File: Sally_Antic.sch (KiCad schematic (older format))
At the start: 0 parts

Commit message: GTIA
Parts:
- added C30, C31: 100nF, Atari:C_Axial_L5.1mm_D2.5mm_P12.50mm_Horizontal, symbol Device:C
- added R31: 3k, Atari:R_Axial_DIN0207_L3.6mm_D2.2mm_P10.16mm_Horizontal, symbol Device:R
- added U18: 74LS08, Package_DIP:DIP-14_W7.62mm_Socket, symbol 74xx:74LS08
- added U7: Antic, Package_DIP:DIP-40_W15.24mm_Socket, symbol Atari:Antic
- added U8: Sally, Package_DIP:DIP-40_W15.24mm_Socket, symbol Atari:Sally
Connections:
- new net: U18.4, U18.5, U7.34 (O0)
- new net: R31.2, U7.6 (~RNMI)
- new net +5VA: C30.1, C31.1, R31.1, U7.21 (VCC), U8.8 (VCC)
- new net A0: U7.13 (A0), U8.9 (A0)
- new net A1: U7.12 (A1), U8.10 (A1)
- new net A10: U7.16 (A10), U8.19 (A10)
- new net A11: U7.22 (A11), U8.20 (A11)
- new net A12: U7.17 (A12), U8.22 (A12)
- new net A13: U7.18 (A13), U8.23 (A13)
- new net A14: U7.19 (A14), U8.24 (A14)
- new net A15: U7.20 (A15), U8.25 (A15)
- new net A2: U7.11 (A2), U8.11 (A2)
- new net A3: U7.10 (A3), U8.12 (A3)
- new net A4: U7.28 (A4), U8.13 (A4)
- new net A5: U7.27 (A5), U8.14 (A5)
- new net A6: U7.26 (A6), U8.15 (A6)
- new net A7: U7.25 (A7), U8.16 (A7)
- new net A8: U7.24 (A8), U8.17 (A8)
- new net A9: U7.23 (A9), U8.18 (A9)
- new net AN0: U7.2 (AN0)
- new net AN1: U7.3 (AN1)
- new net AN2: U7.5 (AN2)
- new net BO2: U7.29 (O2)
- new net D0: U7.30 (D0), U8.33 (D0)
- new net D1: U7.31 (D1), U8.32 (D1)
- new net D2: U7.32 (D2), U8.31 (D2)
- new net D3: U7.33 (D3), U8.30 (D3)
- new net D4: U7.40 (D4), U8.29 (D4)
- new net D5: U7.39 (D5), U8.28 (D5)
- new net D6: U7.38 (D6), U8.27 (D6)
- new net D7: U7.37 (D7), U8.26 (D7)
- new net GND: C30.2, C31.2, U7.1 (VSS), U8.1 (VSS), U8.21 (VSS), U8.38 (S0)
- new net HALT: U7.9 (~HALT), U8.35 (~HALT)
- new net IRQ: U8.4 (~IRQ)
- new net LP: U7.4 (~LP)
- new net NMI: U7.7 (~NMI), U8.6 (~NMI)
- new net O0: U18.6, U8.37 (O0)
- new net O1: U8.3 (O1)
- new net O2: U8.39 (O2)
- new net RDY: U7.15 (RDY), U8.2 (RDY)
- new net REF: U7.8 (~REF)
- new net RST: U7.36 (RST), U8.40 (~RST)
- new net RW: U7.14 (R/~W), U8.36 (R/~W)
- no-connect marks 0 -> 1

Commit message: MMU, Joy, Cart and Video
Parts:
- added R21, R22, R34: 3k, Atari:R_Axial_DIN0207_L3.6mm_D2.2mm_P10.16mm_Horizontal, symbol Device:R
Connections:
- net +5VA: now also R21.1, R22.1, R34.1
- net IRQ: now also R22.2
- net NMI: now also R21.2
- net RDY: now also R34.2
- net RNMI: now reaches R31.2, U7.6 (~RNMI)
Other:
- moved on the sheet: R31
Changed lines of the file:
@@
 $Descr A4 11693 8268
 encoding utf-8
-Sheet 8 14
+Sheet 8 15
 Title ""
 Date ""
@@
 L Device:R R31
 U 1 1 6072AE12
-P 6350 1225
-F 0 "R31" H 6420 1271 50  0000 L CNN
-F 1 "3k" H 6420 1180 50  0000 L CNN
-F 2 "Atari:R_Axial_DIN0207_L3.6mm_D2.2mm_P10.16mm_Horizontal" V 6280 1225 50  0001 C CNN
-F 3 "~" H 6350 1225 50  0001 C CNN
-	1    6350 1225
+P 1925 1525
+F 0 "R31" H 1995 1571 50  0000 L CNN
+F 1 "3k" H 1995 1480 50  0000 L CNN
+F 2 "Atari:R_Axial_DIN0207_L3.6mm_D2.2mm_P10.16mm_Horizontal" V 1855 1525 50  0001 C CNN
+F 3 "~" H 1925 1525 50  0001 C CNN
+	1    1925 1525
 	1    0    0    -1
 $EndComp
@@
 L power:+5VA #PWR0157
 U 1 1 6072B622
-P 6350 950
-F 0 "#PWR0157" H 6350 800 50  0001 C CNN
-F 1 "+5VA" H 6365 1123 50  0000 C CNN
-F 2 "" H 6350 950 50  0001 C CNN
-F 3 "" H 6350 950 50  0001 C CNN
-	1    6350 950
-	1    0    0    -1
-$EndComp
-Wire Wire Line
-	6350 950  6350 1075
-Wire Wire Line
-	6350 1375 6350 2525
-Wire Wire Line
-	6350 2525 6825 2525
+P 1925 1250
+F 0 "#PWR0157" H 1925 1100 50  0001 C CNN
+F 1 "+5VA" H 1940 1423 50  0000 C CNN
+F 2 "" H 1925 1250 50  0001 C CNN
+F 3 "" H 1925 1250 50  0001 C CNN
+	1    1925 1250
+	1    0    0    -1
+$EndComp
 Text GLabel 6825 2825 0    50   Input ~ 0
 REF
@@
 Wire Wire Line
 	9350 4175 9350 5675
+Text GLabel 1025 1650 3    50   Input ~ 0
+RDY
+$Comp
+L Device:R R34
+U 1 1 6026667E
+P 1025 1500
+F 0 "R34" H 1095 1546 50  0000 L CNN
+F 1 "3k" H 1095 1455 50  0000 L CNN
+F 2 "Atari:R_Axial_DIN0207_L3.6mm_D2.2mm_P10.16mm_Horizontal" V 955 1500 50  0001 C CNN
+F 3 "~" H 1025 1500 50  0001 C CNN
+	1    1025 1500
+	1    0    0    -1
+$EndComp
+$Comp
+L power:+5VA #PWR0179
+U 1 1 60266D94
+P 1025 1250
+F 0 "#PWR0179" H 1025 1100 50  0001 C CNN
+F 1 "+5VA" H 1040 1423 50  0000 C CNN
+F 2 "" H 1025 1250 50  0001 C CNN
+F 3 "" H 1025 1250 50  0001 C CNN
+	1    1025 1250
+	1    0    0    -1
+$EndComp
+Wire Wire Line
+	1025 1250 1025 1350
+Text GLabel 1325 1675 3    50   Input ~ 0
+IRQ
+$Comp
+L Device:R R22
+U 1 1 6026797E
+P 1325 1525
+F 0 "R22" H 1395 1571 50  0000 L CNN
+F 1 "3k" H 1395 1480 50  0000 L CNN
+F 2 "Atari:R_Axial_DIN0207_L3.6mm_D2.2mm_P10.16mm_Horizontal" V 1255 1525 50  0001 C CNN
+F 3 "~" H 1325 1525 50  0001 C CNN
+	1    1325 1525
+	1    0    0    -1
+$EndComp
+$Comp
+L power:+5VA #PWR0180
+U 1 1 60267BFA
+P 1325 1250
+F 0 "#PWR0180" H 1325 1100 50  0001 C CNN
+F 1 "+5VA" H 1340 1423 50  0000 C CNN
+F 2 "" H 1325 1250 50  0001 C CNN
+F 3 "" H 1325 1250 50  0001 C CNN
+	1    1325 1250
+	1    0    0    -1
+$EndComp
+Wire Wire Line
+	1325 1250 1325 1375
+Text GLabel 1600 1675 3    50   Input ~ 0
+NMI
+$Comp
+L Device:R R21
+U 1 1 60268FC3
+P 1600 1525
+F 0 "R21" H 1670 1571 50  0000 L CNN
+F 1 "3k" H 1670 1480 50  0000 L CNN
+F 2 "Atari:R_Axial_DIN0207_L3.6mm_D2.2mm_P10.16mm_Horizontal" V 1530 1525 50  0001 C CNN
+F 3 "~" H 1600 1525 50  0001 C CNN
+	1    1600 1525
+	1    0    0    -1
+$EndComp
+$Comp
+L power:+5VA #PWR0181
+U 1 1 602692C7
+P 1600 1250
+F 0 "#PWR0181" H 1600 1100 50  0001 C CNN
+F 1 "+5VA" H 1615 1423 50  0000 C CNN
+F 2 "" H 1600 1250 50  0001 C CNN
+F 3 "" H 1600 1250 50  0001 C CNN
+	1    1600 1250
+	1    0    0    -1
+$EndComp
+Wire Wire Line
+	1600 1250 1600 1375
+Wire Wire Line
+	1925 1250 1925 1375
+Text GLabel 6825 2525 0    50   Input ~ 0
+RNMI
+Text GLabel 1925 1675 3    50   Input ~ 0
+RNMI
 $EndSCHEMATC

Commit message: PIA and POKEY
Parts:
- added R33: 3k, Atari:R_Axial_DIN0207_L3.6mm_D2.2mm_P10.16mm_Horizontal, symbol Device:R
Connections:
- net +5VA: now also R33.1
- net LP: now also R33.2
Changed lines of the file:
@@
 Text GLabel 1925 1675 3    50   Input ~ 0
 RNMI
+Text GLabel 2225 1675 3    50   Input ~ 0
+LP
+$Comp
+L Device:R R33
+U 1 1 6041696A
+P 2225 1525
+F 0 "R33" H 2295 1571 50  0000 L CNN
+F 1 "3k" H 2295 1480 50  0000 L CNN
+F 2 "Atari:R_Axial_DIN0207_L3.6mm_D2.2mm_P10.16mm_Horizontal" V 2155 1525 50  0001 C CNN
+F 3 "~" H 2225 1525 50  0001 C CNN
+	1    2225 1525
+	1    0    0    -1
+$EndComp
+$Comp
+L power:+5VA #PWR0223
+U 1 1 60416BF5
+P 2225 1250
+F 0 "#PWR0223" H 2225 1100 50  0001 C CNN
+F 1 "+5VA" H 2240 1423 50  0000 C CNN
+F 2 "" H 2225 1250 50  0001 C CNN
+F 3 "" H 2225 1250 50  0001 C CNN
+	1    2225 1250
+	1    0    0    -1
+$EndComp
+Wire Wire Line
+	2225 1250 2225 1375
 $EndSCHEMATC

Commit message: Tracking
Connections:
- net FO0: now reaches U7.35 (FO0)
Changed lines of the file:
@@
 Wire Wire Line
 	2225 1250 2225 1375
+Text GLabel 8025 2475 2    50   Input ~ 0
+FO0
 $EndSCHEMATC

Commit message: Tracking
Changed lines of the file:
@@
 $EndDescr
-$Comp
-L Atari:Sally U8
-U 1 1 6071A1A8
-P 4100 3525
-F 0 "U8" H 4100 5280 50  0000 C CNN
-F 1 "Sally" H 4100 5189 50  0000 C CNN
-F 2 "Package_DIP:DIP-40_W15.24mm_Socket" H 4100 5098 50  0000 C CNN
-F 3 "" H 4100 3525 50  0001 C CNN
-	1    4100 3525
-	1    0    0    -1
-$EndComp
 $Comp
 L Atari:Antic U7
@@
 O1
 Wire Wire Line
-	4700 4825 4700 4925
-Connection ~ 4700 4925
-Wire Wire Line
 	3500 2125 3075 2125
 Wire Wire Line
@@
 Wire Wire Line
 	3500 2425 3075 2425
-Connection ~ 3500 2425
 Wire Wire Line
 	3075 1975 3075 2125
@@
 	3075 2425 3075 2500
 Connection ~ 3075 2425
-Wire Wire Line
-	4700 4925 4700 5225
 Text GLabel 4700 2325 2    50   Input ~ 0
 RDY
@@
 Text GLabel 8025 2475 2    50   Input ~ 0
 FO0
+Wire Wire Line
+	4700 4825 4700 4925
+$Comp
+L Atari:Sally U8
+U 1 1 603A2980
+P 4100 3525
+F 0 "U8" H 4100 5280 50  0000 C CNN
+F 1 "Sally" H 4100 5189 50  0000 C CNN
+F 2 "Package_DIP:DIP-40_W15.24mm_Socket" H 4100 5098 50  0000 C CNN
+F 3 "" H 4100 3525 50  0001 C CNN
+	1    4100 3525
+	1    0    0    -1
+$EndComp
+Wire Wire Line
+	4700 4925 4700 5225
+Connection ~ 4700 4925
 $EndSCHEMATC

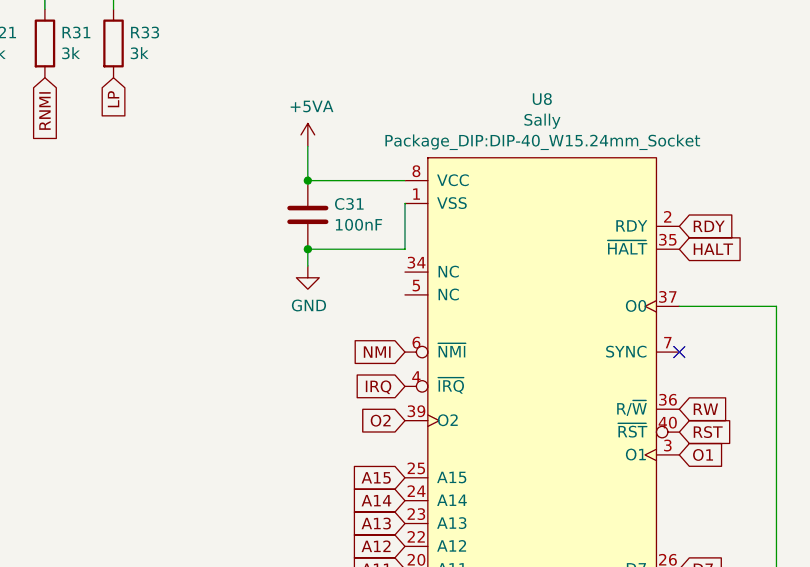
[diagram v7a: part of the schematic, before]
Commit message: Diagnostic pin
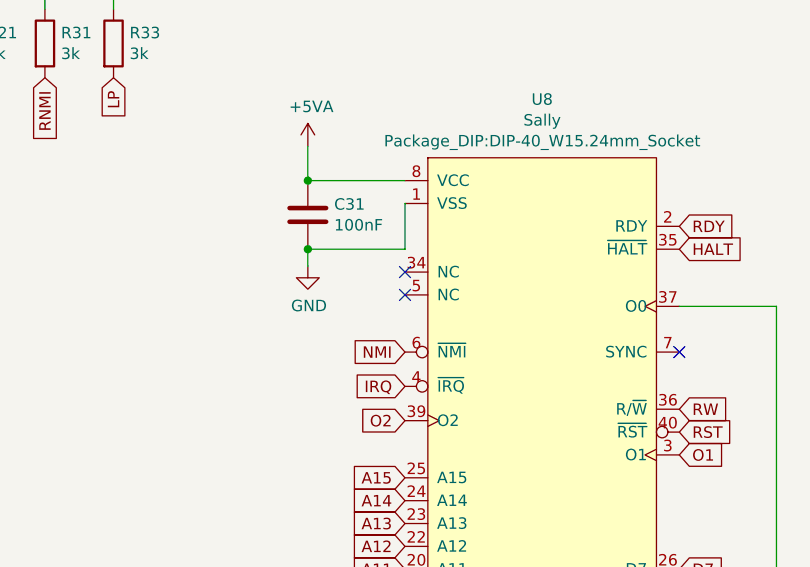
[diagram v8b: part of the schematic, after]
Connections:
- no-connect marks 1 -> 3
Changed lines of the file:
@@
 Wire Wire Line
 	4700 4825 4700 4925
+Wire Wire Line
+	4700 4925 4700 5225
+Connection ~ 4700 4925
 $Comp
 L Atari:Sally U8
-U 1 1 603A2980
+U 1 1 6048F641
 P 4100 3525
-AR Path="/603A2980" Ref="U8"  Part="1"
-AR Path="/60205A08/603A2980" Ref="U8"  Part="1"
 F 0 "U8" H 4100 5280 50  0000 C CNN
 F 1 "Sally" H 4100 5189 50  0000 C CNN
@@
 	1    0    0    -1
 $EndComp
-Wire Wire Line
-	4700 4925 4700 5225
-Connection ~ 4700 4925
+NoConn ~ 3500 2525
+NoConn ~ 3500 2625
 $EndSCHEMATC
